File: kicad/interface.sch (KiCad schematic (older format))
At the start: 32 parts, among them J1 Conn_02x05_Odd_Even, J2 Conn_02x20_Odd_Even, J3 Conn_02x05_Odd_Even, J7 Conn_01x02, U1 24LC32, U4 NUP4114UPXV6T1G, U5 NB3L553

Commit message: add modeles to 3d render
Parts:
- D2: footprint (none) -> library:EQFP-144_20x20mm_Pitch0.5mm
- J2: footprint Pin_Headers:Pin_Header_Straight_2x20_Pitch2.54mm -> Socket_Strips:Socket_Strip_Straight_2x20_Pitch2.54mm
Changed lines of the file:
@@
 F 0 "J2" H 6450 3000 50  0000 C CNN
 F 1 "Conn_02x20_Odd_Even" H 6450 900 50  0000 C CNN
-F 2 "Pin_Headers:Pin_Header_Straight_2x20_Pitch2.54mm" H 6400 2000 50  0001 C CNN
+F 2 "Socket_Strips:Socket_Strip_Straight_2x20_Pitch2.54mm" H 6400 2000 50  0001 C CNN
 F 3 "" H 6400 2000 50  0001 C CNN
 	1    6400 2000
@@
 F 0 "D2" H 10100 2950 60  0000 C CNN
 F 1 "10cl025" H 10650 2950 60  0000 C CNN
-F 2 "" H 9450 2350 60  0001 C CNN
+F 2 "library:EQFP-144_20x20mm_Pitch0.5mm" H 9450 2350 60  0001 C CNN
 F 3 "" H 9450 2350 60  0001 C CNN
 	1    10450 2000
@@
 F 0 "D2" H 6100 6250 60  0000 C CNN
 F 1 "10cl025" H 6700 6250 60  0000 C CNN
-F 2 "" H 5450 6150 60  0001 C CNN
+F 2 "library:EQFP-144_20x20mm_Pitch0.5mm" H 5450 6150 60  0001 C CNN
 F 3 "" H 5450 6150 60  0001 C CNN
 	2    6450 5800
@@
 F 0 "D2" H 10100 6150 60  0000 C CNN
 F 1 "10cl025" H 10700 6150 60  0000 C CNN
-F 2 "" H 9450 5950 60  0001 C CNN
+F 2 "library:EQFP-144_20x20mm_Pitch0.5mm" H 9450 5950 60  0001 C CNN
 F 3 "" H 9450 5950 60  0001 C CNN
 	3    10450 5600
@@
 F 0 "D2" H 6100 5050 60  0000 C CNN
 F 1 "10cl025" H 6700 5050 60  0000 C CNN
-F 2 "" H 5450 4850 60  0001 C CNN
+F 2 "library:EQFP-144_20x20mm_Pitch0.5mm" H 5450 4850 60  0001 C CNN
 F 3 "" H 5450 4850 60  0001 C CNN
 	5    6450 4500
@@
 F 0 "D2" H 10100 4750 60  0000 C CNN
 F 1 "10cl025" H 10700 4750 60  0000 C CNN
-F 2 "" H 9450 4350 60  0001 C CNN
+F 2 "library:EQFP-144_20x20mm_Pitch0.5mm" H 9450 4350 60  0001 C CNN
 F 3 "" H 9450 4350 60  0001 C CNN
 	6    10450 4000
@@
 F 3 "" H 2200 3150 50  0001 C CNN
 	1    2200 3150
-	1    0    0    -1
-$EndComp
-$Comp
-L CFPS-73 G1
-U 1 1 5AD09F7E
-P 1800 6950
-F 0 "G1" H 1650 7200 60  0000 C CNN
-F 1 "CFPS-73" H 1800 6700 60  0000 C CNN
-F 2 "library:CFPS-73" H 1800 6950 60  0001 C CNN
-F 3 "" H 1800 6950 60  0001 C CNN
-	1    1800 6950
 	1    0    0    -1
 $EndComp
@@
 	3800 7550 3800 7500
 Connection ~ 3300 7550
+$Comp
+L CFPS-73 G1
+U 1 1 5B06B8DD
+P 1800 6950
+F 0 "G1" H 1650 7200 60  0000 C CNN
+F 1 "CFPS-73" H 1800 6700 60  0000 C CNN
+F 2 "library:CFPS-73" H 1800 6950 60  0001 C CNN
+F 3 "" H 1800 6950 60  0001 C CNN
+	1    1800 6950
+	1    0    0    -1
+$EndComp
 $EndSCHEMATC

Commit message: Project translated to template "Raspberry Pi HAT" Added library files from template. Renamed refdes. Changed placement for all components
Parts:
- removed J2: Conn_02x20_Odd_Even, Socket_Strips:Socket_Strip_Straight_2x20_Pitch2.54mm, symbol Conn_02x20_Odd_Even
- added J3: OX40HAT, Socket_Strips:Socket_Strip_Straight_2x20_Pitch2.54mm, symbol OX40HAT
- renumbered C6 to C1, C5 to C2, C45 to C3, D10 to D2, D11 to D3, D12 to D6, D2 to D7, J3 to J1, J7 to J2, J1 to J4, R18 to R1, R1 to R10, R2 to R11, R3 to R12, R19 to R13, R20 to R14, R15 to R2, R16 to R3, R32 to R4, R33 to R5, R17 to R6, R4 to R7, R5 to R8, R6 to R9, U4 to U2, U5 to U3

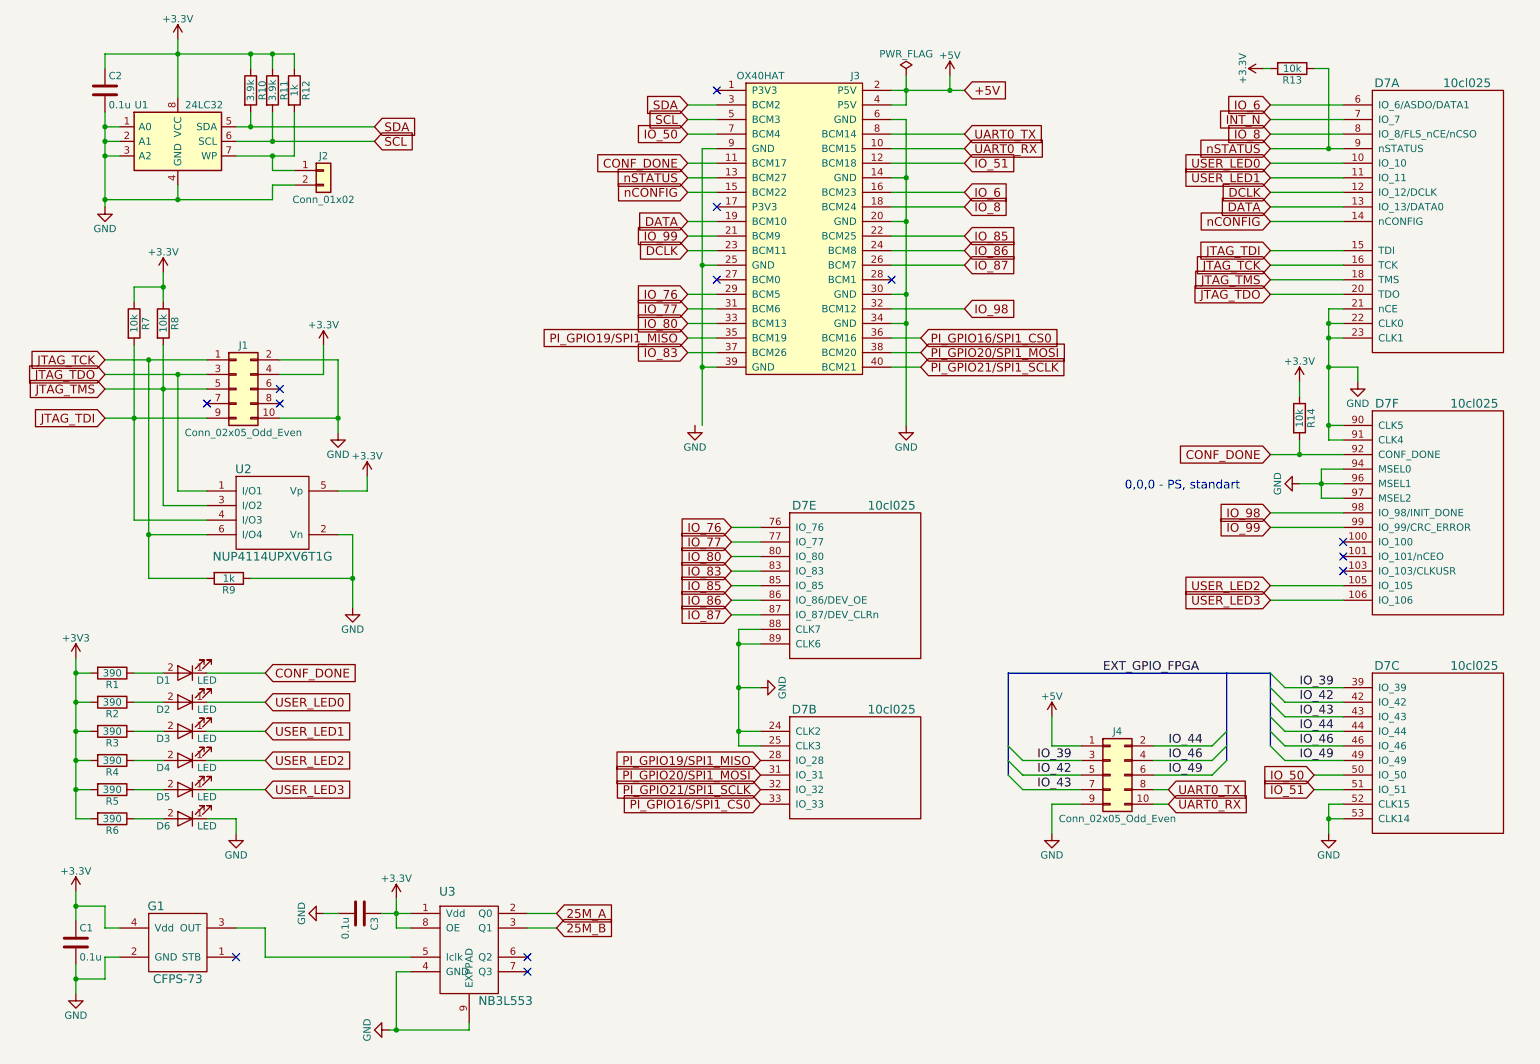
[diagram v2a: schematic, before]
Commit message: Schematics updated for correct BOM generation Corrected RefDes (not renumbered yet) PCB updated (not routed) Added 3d models for new components Added folder assy (empty) Added folder bom Added BOM file (bom/BOM_fpgagigepi.xls) Added datasheet for ocscillator 25MHz (datasheets/ASEMB.pdf)
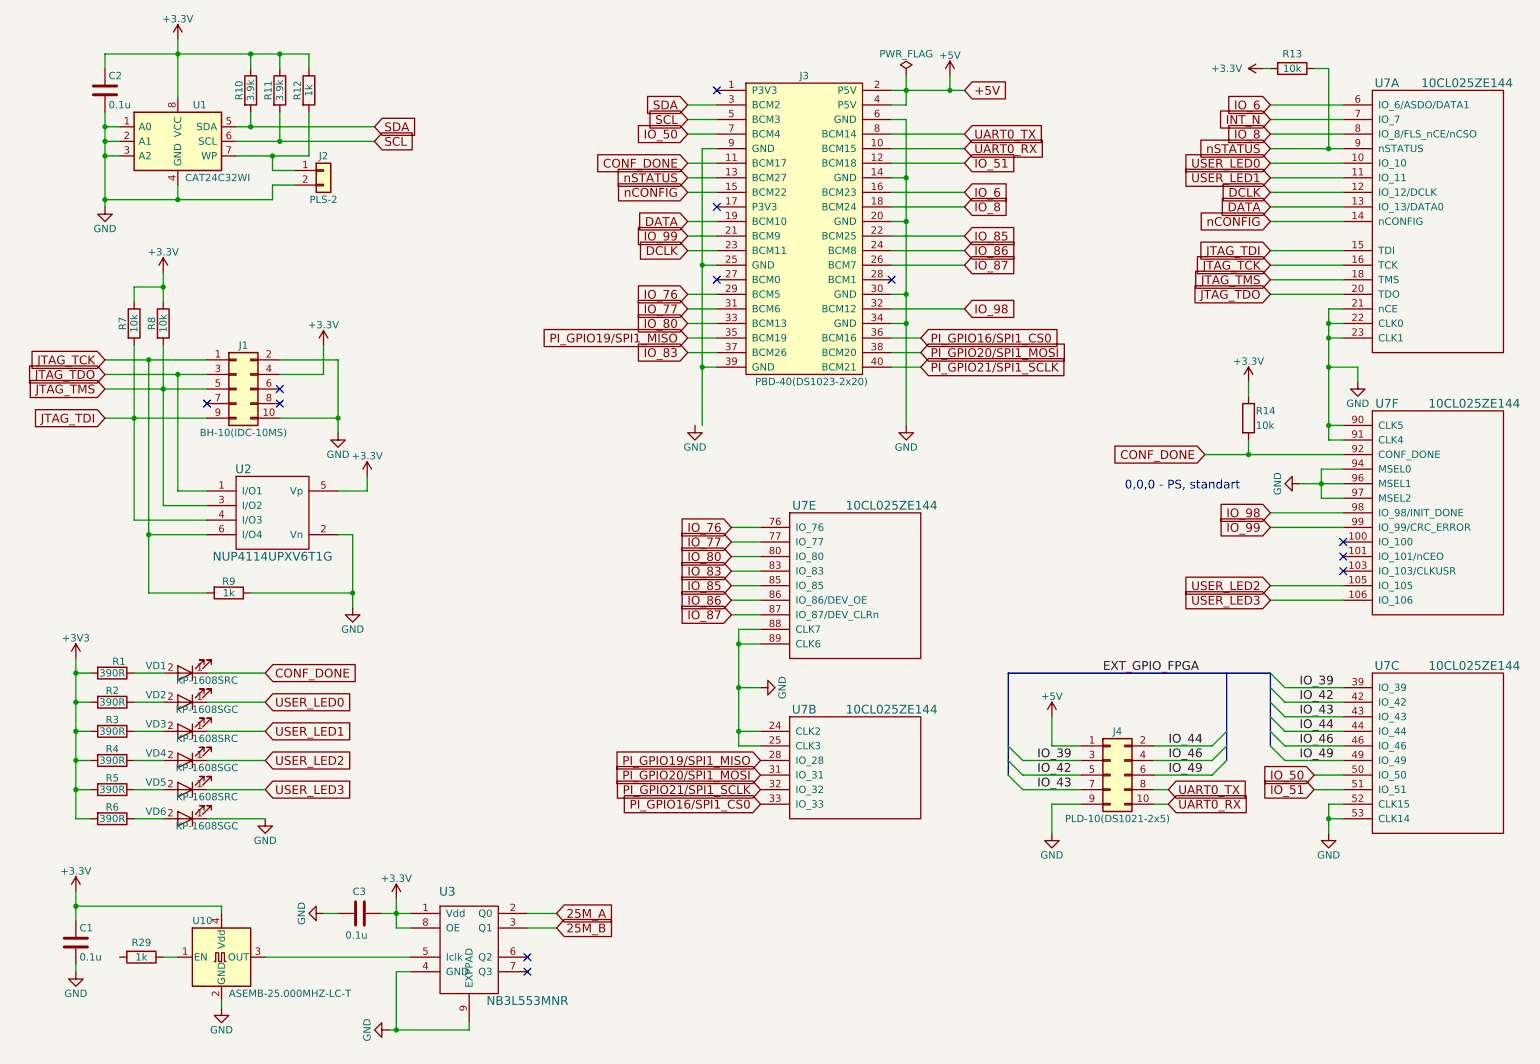
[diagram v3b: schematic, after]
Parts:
- removed G1: CFPS-73, library:CFPS-73, symbol CFPS-73
- added R29: 1k, Resistors_SMD:R_0603, symbol R
- added U10: ASEMB-25.000MHZ-LC-T, Oscillators:Oscillator_SMD_Abracon_ASE-4pin_3.2x2.5mm, symbol ASE-xxxMHz
- C1, C2, C3: footprint Capacitors_SMD:C_0603_HandSoldering -> Capacitors_SMD:C_0603
- J1: value Conn_02x05_Odd_Even -> BH-10(IDC-10MS); footprint Pin_Headers:Pin_Header_Straight_2x05_Pitch2.54mm -> Connectors_IDC:IDC-Header_2x05_Pitch2.54mm_Straight
- J2: value Conn_01x02 -> PLS-2
- J3: value OX40HAT -> PBD-40(DS1023-2x20)
- J4: value Conn_02x05_Odd_Even -> PLD-10(DS1021-2x5)
- R1, R2, R3, R4, R5, R6: value 390 -> 390R; footprint Resistors_SMD:R_0603_HandSoldering -> Resistors_SMD:R_0603
- R10, R11, R12, R13, R14, R7, R8, R9: footprint Resistors_SMD:R_0603_HandSoldering -> Resistors_SMD:R_0603
- U1: value 24LC32 -> CAT24C32WI
- U3: value NB3L553 -> NB3L553MNR
- U7: renamed from D7; value 10cl025 -> 10CL025ZE144; PartNumber (none) -> CL
- U7: renamed from D7; value 10cl025 -> 10CL025ZE144
- VD1: renamed from D1; value LED -> KP-1608SRC; footprint LEDs:LED_0603_HandSoldering -> LEDs:LED_0603
- VD2: renamed from D2; value LED -> KP-1608SGC; footprint LEDs:LED_0603_HandSoldering -> LEDs:LED_0603
- VD3: renamed from D3; value LED -> KP-1608SRC; footprint LEDs:LED_0603_HandSoldering -> LEDs:LED_0603
- VD4: renamed from D4; value LED -> KP-1608SGC; footprint LEDs:LED_0603_HandSoldering -> LEDs:LED_0603
- VD5: renamed from D5; value LED -> KP-1608SRC; footprint LEDs:LED_0603_HandSoldering -> LEDs:LED_0603
- VD6: renamed from D6; value LED -> KP-1608SGC; footprint LEDs:LED_0603_HandSoldering -> LEDs:LED_0603
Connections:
- net +3V3: now also U10.4 (Vdd)
- net GND: now also U10.2 (GND)
- net at U3.5 (Iclk): now also U10.3 (OUT)
- new net: R29.1, U10.1 (EN)
- no-connect marks 13 -> 12
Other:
- moved on the sheet: R11, R12, R14, R9
